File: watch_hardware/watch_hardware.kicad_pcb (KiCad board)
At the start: 4 copper layers, 31.7 x 39.6 mm, 102 parts, among them J1 USB_C_Receptacle_USB2.0_16P, J2 TF_Card, Q1 PMOS, SW1 SW_Push, SW2 SW_Push, SW3 SW_Push, SW4 SW_Push, U1 ESP32-S3, U10 LM2664, U11 TPS65217, U2 TK018F3716, U3 W25Q128JVP, U4 LIS3MDL, U5 LSM6DSOW, U6 AW9523B, U7 LPS22HB, U8 CJC4344H, U9 OPA2192, Y1 Crystal_GND24

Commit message: daily
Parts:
- C11, C15, C16, C22, C26, C4: footprint Capacitor_SMD:C_0603_1608Metric -> Capacitor_SMD:C_0402_1005Metric
- C18, C19, C21, C27, C29, C34, C36, D1, R12, R13, R14, R16, R17, R18, R19, R4, R5, U9: moved to B.Cu
- C28: footprint Capacitor_SMD:C_0603_1608Metric -> Capacitor_SMD:C_0402_1005Metric; moved to B.Cu
- LS1: footprint Connector_PinHeader_1.27mm:PinHeader_1x02_P1.27mm_Vertical -> Connector_PinHeader_1.00mm:PinHeader_1x02_P1.00mm_Vertical
- moved C13 81.5 mm to (192.4, 74.2)
- moved C14 81.5 mm to (192.4, 76.1)
- moved C15 79.4 mm to (192.6, 79.8)
- moved C24 74.9 mm to (187.3, 78.7)
- moved C22 73.3 mm to (187.2, 81.9)
- moved C38 72.3 mm to (170.8, 47.1), turned to 90 degrees
- moved R7 71.2 mm to (166.3, 86.6)
- moved R8 71.2 mm to (166.3, 88.6)
- moved C39 70.1 mm to (167.1, 53.4), turned to 90 degrees
- moved R17 69.5 mm to (170.0, 52.4)
- moved R16 69.3 mm to (170.0, 51.4), turned to 180 degrees
- moved C40 69.2 mm to (165.6, 53.4), turned to 90 degrees
- moved R5 69.1 mm to (165.0, 67.4), turned to -90 degrees
- moved C42 69.1 mm to (167.1, 50.4), turned to -90 degrees
- moved R4 68.6 mm to (164.3, 63.5), turned to 180 degrees
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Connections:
- C19 pad 1: Net-(C19-Pad1) -> GND
- R12 pad 2: Net-(C19-Pad1) -> GND
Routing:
- net +3.3V: track 0.00 -> 57.4 mm, vias 0 -> 2
- net +5V: track 0.00 -> 35.1 mm, vias 0 -> 2
- net +1V0: track 0.00 -> 33.1 mm, vias 0 -> 1
- net +3V3: track 21.5 -> 52.9 mm, vias 7 -> 12
- net /SYS: track 0.00 -> 24.7 mm, vias 0 -> 4
- net +2V0: track 0.00 -> 21.1 mm, vias 0 -> 1
- net -3V3: track 0.00 -> 20.7 mm, vias 0 -> 1
- net Net-(BT1-+): track 0.00 -> 18.8 mm
- net Net-(U11-VDCDC1): track 0.00 -> 18.2 mm
- net Net-(U11-PB_IN): track 0.00 -> 17.1 mm, vias 0 -> 1
- net /-IN_A: track 0.00 -> 14.2 mm
- net Net-(U11-TS): track 0.00 -> 8.89 mm
- net Net-(U11-L1): track 0.00 -> 7.37 mm
- net /+IN_A: track 0.00 -> 7.01 mm
- net Net-(U1-GPIO46): track 1.83 -> 8.54 mm, vias 1 -> 0
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- added copper zone on F.Cu, net Net-(U11-L2)

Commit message: daily
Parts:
- added SCL0: TestPoint, projects:testpoint, B.Cu at (165.9, 49.6)
- added SDA0: TestPoint, projects:testpoint, B.Cu at (165.9, 51.0)
- C1, C2, C3, R1, R2, R3: moved to B.Cu
- SW1, SW2, SW3, SW4: footprint Connector_PinHeader_1.00mm:PinHeader_1x02_P1.00mm_Vertical -> projects:switch_base; moved to B.Cu
- U11: value TPS65217 -> TPS652170
- moved SW4 11.6 mm to (163.2, 47.9)
- moved R2 4.35 mm to (156.5, 81.6), turned to 180 degrees
- moved C3 4.02 mm to (160.3, 80.5), turned to 180 degrees
- moved SW3 3.35 mm to (159.5, 83.1), turned to 180 degrees
- moved R1 2.92 mm to (152.8, 81.7), turned to 180 degrees
- moved C2 2.62 mm to (156.6, 80.5), turned to 180 degrees
- moved SW2 2.15 mm to (155.8, 83.1), turned to 180 degrees
- moved R3 1.86 mm to (160.2, 81.6), turned to 180 degrees
- moved C1 1.52 mm to (152.9, 80.6), turned to 180 degrees
- moved SW1 1.17 mm to (152.1, 83.1), turned to 180 degrees
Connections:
- C39 pad 2: Net-(U11-VDCDC1) -> +3.3V
- C40 pad 2: Net-(U11-VDCDC1) -> +3.3V
- C43 pad 2: +1V0 -> +3.3VDAC
- C44 pad 2: +1V0 -> +3.3VDAC
- L2 pad 1: Net-(U11-VDCDC1) -> +3.3V
- L4 pad 2: +1V0 -> +3.3VDAC
- U11 pad 19: Net-(U11-VDCDC1) -> +3.3V
- U11 pad 29: +1V0 -> +3.3VDAC
- U11 pad 39: +3V3 -> unconnected-(U11-LS1_IN-Pad39)
- U11 pad 40: +3.3VDAC -> unconnected-(U11-LS1_OUT-Pad40)
- U11 pad 42: +3V3 -> unconnected-(U11-LS2_IN-Pad42)
- U11 pad 43: +3.3V -> unconnected-(U11-LS2_OUT-Pad43)
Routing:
- net /L_CS: track 2.13 -> 20.6 mm
- net Net-(U11-PB_IN): track 17.1 -> 6.65 mm
- net /L_RST: track 2.04 -> 11.3 mm
- net /SDA0: track 6.59 -> 12.6 mm
- net /SCL0: track 6.55 -> 12.1 mm
- net +3V3: track 52.9 -> 48.6 mm
- net unconnected-(U11-LS2_IN-Pad42): track 0.00 -> 3.29 mm
- net unconnected-(U11-LS1_OUT-Pad40): track 0.00 -> 2.90 mm
- net +3.3VDAC: track 6.05 -> 3.15 mm
- net /L_D1: track 13.8 -> 16.2 mm
- net unconnected-(U11-LS1_IN-Pad39): track 0.00 -> 1.00 mm
- net GND: vias 74 -> 73

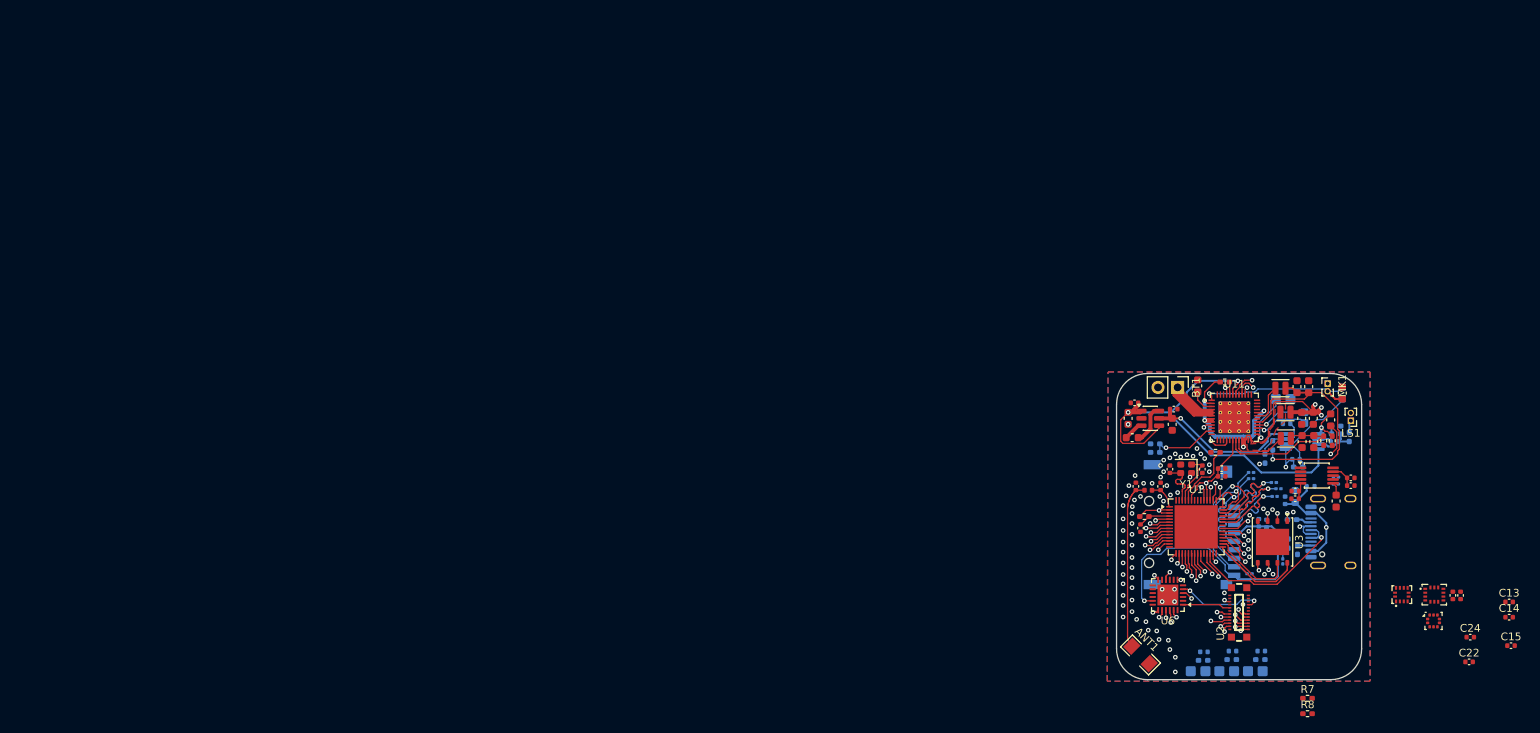
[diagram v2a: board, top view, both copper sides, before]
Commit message: 准备添加卫星定位
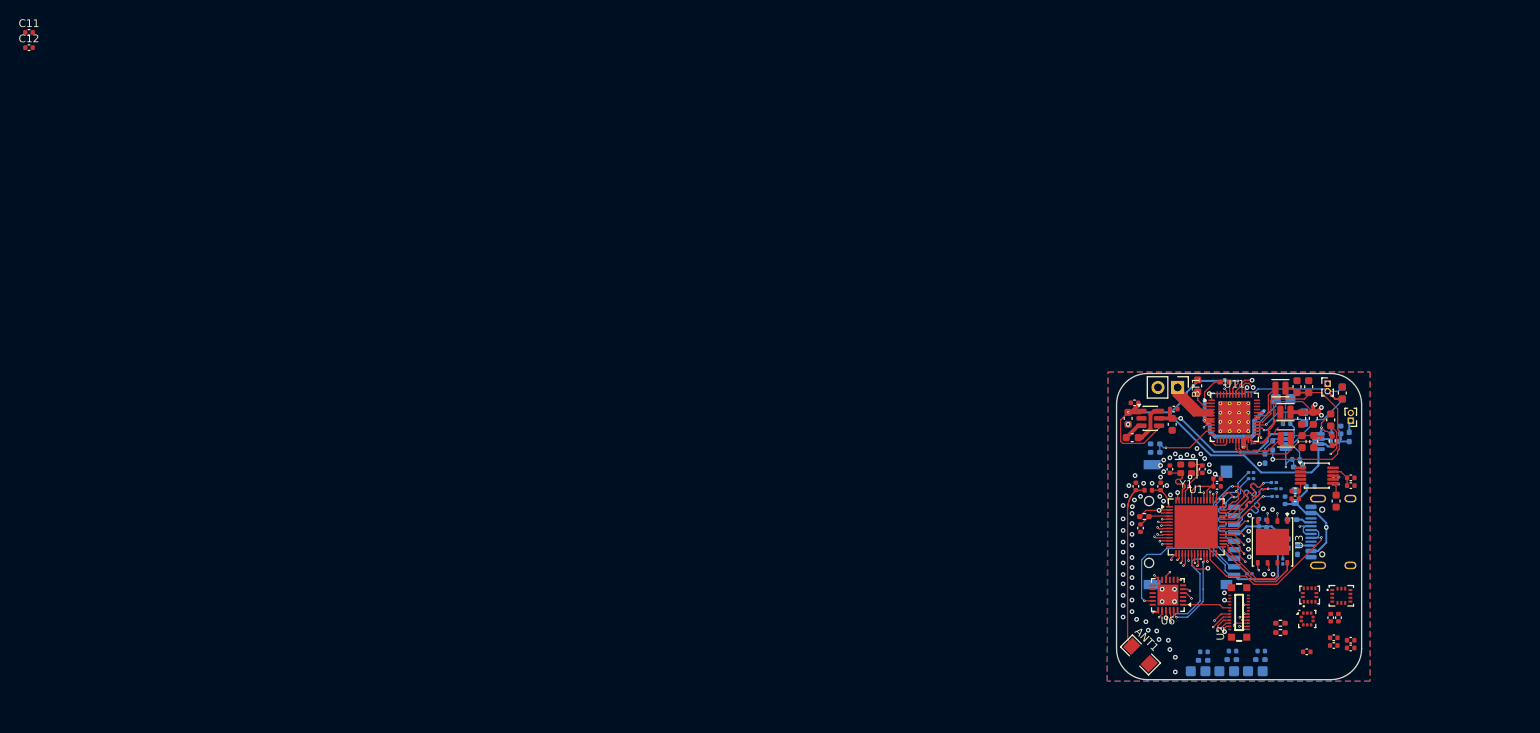
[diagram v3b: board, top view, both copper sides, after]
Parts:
- removed the R11 at (154.4, 54.8)
- removed R22: 10k, Resistor_SMD:R_0402_1005Metric_Pad0.72x0.64mm_HandSolder
- added C11: 100nF, Capacitor_SMD:C_0402_1005Metric, F.Cu at (0.94, 0.48)
- added C12: 10uF, Capacitor_SMD:C_0402_1005Metric, F.Cu at (0.94, 2.46)
- R10: renamed from R13; value 82k -> 270k
- moved C15 27.0 mm to (166.2, 80.6)
- moved C17 20.7 mm to (171.9, 80.1)
- moved C16 20.7 mm to (171.9, 79.1)
- moved C26 17.7 mm to (169.7, 78.8)
- moved C24 17.6 mm to (169.7, 79.8)
- moved U7 16.3 mm to (166.3, 76.3)
- moved C13 16.1 mm to (170.3, 76.2)
- moved C14 16.1 mm to (169.3, 76.2)
- moved U5 12.0 mm to (170.7, 73.3)
- moved U4 11.9 mm to (166.6, 73.2)
- moved R8 11.1 mm to (162.8, 78.1)
- moved R7 10.3 mm to (162.8, 76.9)
- moved C4 1.43 mm to (154.6, 58.2)
- moved C6 1.43 mm to (154.6, 59.2)
- renumbered C11 to C13, C12 to C14, C13 to C15, C14 to C16, C15 to C17, C16 to C18, C17 to C19, C18 to C20, C19 to C21, C20 to C22, C21 to C23, C22 to C24, C23 to C25, C24 to C26, C25 to C27, C26 to C28, C27 to C29, C28 to C30, C29 to C31, C30 to C32, C31 to C33, C32 to C34, C33 to C35, C34 to C36, C35 to C37, C36 to C38, C37 to C39, C38 to C40, C39 to C41, C40 to C42, C41 to C43, C42 to C44, C43 to C45, C44 to C46, R14 to R11, R15 to R12, R16 to R13, R17 to R14, R18 to R15, R19 to R16, R20 to R17, R21 to R18, R12 to R9, SCL0 to SCL1, SDA0 to SDA1
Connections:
- C16 pad 1: +3.3VA -> +3.3VP
- C17 pad 1: +3.3VA -> +3.3VP
- C24 pad 1: +3.3VA -> +3.3VP
- C26 pad 1: +3.3VA -> +3.3VP
- R10 pad 1: +1V0 -> +2V0
- U1 pad 20: +3V3 -> +3.3VA
- U1 pad 24: unconnected-(U1-GPIO18-Pad24) -> /AW_RST
- U1 pad 27: /AW_RST -> unconnected-(U1-GPIO21-Pad27)
- U1 pad 52: Net-(U1-GPIO46) -> GND
- U11 pad 39: unconnected-(U11-LS1_IN-Pad39) -> +3V3
- U11 pad 40: unconnected-(U11-LS1_OUT-Pad40) -> +3.3VP
- U4 pad 10: +3.3VA -> +3.3VP
- U4 pad 5: +3.3VA -> +3.3VP
- U4 pad 6: +3.3VA -> +3.3VP
- U5 pad 5: +3.3VA -> +3.3VP
- U7 pad 1: +3.3VA -> +3.3VP
- U7 pad 10: +3.3VA -> +3.3VP
- U7 pad 6: +3.3VA -> +3.3VP
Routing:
- net +1V0: track 33.1 -> 0.00 mm, vias 1 -> 0
- net (no net): track 0.00 -> 33.1 mm
- net +3.3V: track 57.4 -> 75.6 mm
- net Net-(U11-VDCDC1): track 18.2 -> 0.00 mm
- net /L_RST: track 11.3 -> 1.53 mm
- net /AW_INT: track 4.90 -> 14.5 mm
- net /AW_RST: track 2.28 -> 11.6 mm
- net Net-(U1-GPIO46): track 8.54 -> 0.00 mm
- net +3V3: track 48.6 -> 42.3 mm, vias 12 -> 11
- net /L_CS: track 20.6 -> 16.4 mm
- net +3.3VA: track 3.20 -> 7.03 mm, vias 0 -> 1
- net /L_MOSI: track 19.3 -> 15.5 mm
- net unconnected-(U11-LS1_OUT-Pad40): track 2.90 -> 0.00 mm
- net +3.3VP: track 0.00 -> 2.90 mm
- net /GPIO2: track 3.20 -> 1.08 mm
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
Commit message: 完成电路设计
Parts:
- removed C11: 100nF, Capacitor_SMD:C_0402_1005Metric
- removed C12: 10uF, Capacitor_SMD:C_0402_1005Metric
- added AE1: IPEX_1, projects:IPEX_1, F.Cu at (167.7, 82.1)
- added C32: 100nF, Capacitor_SMD:C_0402_1005Metric, B.Cu at (165.0, 81.2)
- added C33: 470pF, Capacitor_SMD:C_0402_1005Metric, B.Cu at (166.7, 81.9)
- added C34: 100nF, Capacitor_SMD:C_0402_1005Metric, B.Cu at (167.7, 78.2)
- added C35: 470pF, Capacitor_SMD:C_0402_1005Metric, B.Cu at (159.6, 76.1)
- added C37: 10nF, Capacitor_SMD:C_0402_1005Metric, B.Cu at (167.3, 74.5)
- added C38: 10nF, Capacitor_SMD:C_0402_1005Metric, B.Cu at (168.9, 72.4)
- added C40: 100nF, Capacitor_SMD:C_0402_1005Metric, B.Cu at (166.6, 73.0)
- added C41: 100nF, Capacitor_SMD:C_0402_1005Metric, B.Cu at (166.6, 71.5)
- added C42: 470pF, Capacitor_SMD:C_0402_1005Metric, B.Cu at (163.9, 71.1)
- added C43: 100nF, Capacitor_SMD:C_0402_1005Metric, B.Cu at (162.1, 71.3)
- added C44: 100nF, Capacitor_SMD:C_0402_1005Metric, B.Cu at (159.0, 77.6)
- added C45: 10nF, Capacitor_SMD:C_0402_1005Metric, B.Cu at (160.0, 77.6)
- added L2: 47nH, Inductor_SMD:L_0402_1005Metric, B.Cu at (167.7, 81.9)
- added R17: 20k, Resistor_SMD:R_0402_1005Metric_Pad0.72x0.64mm_HandSolder, B.Cu at (163.8, 72.1)
- added U10: MAX2769C, Package_DFN_QFN:QFN-28-1EP_5x5mm_P0.5mm_EP3.25x3.25mm_ThermalVias, B.Cu at (163.7, 77.1)
- added Y2: 7Q16300001, Crystal:Crystal_SMD_3225-4Pin_3.2x2.5mm, B.Cu at (170.2, 75.5)
- C39: value 10uF -> 27pF; footprint Capacitor_SMD:C_0603_1608Metric -> Capacitor_SMD:C_0402_1005Metric; moved to B.Cu
- moved C39 29.4 mm to (163.9, 73.1), turned to 180 degrees
- moved C54 18.7 mm to (152.1, 46.2)
- moved C24 9.58 mm to (160.7, 76.5), turned to -90 degrees
- moved D2 8.60 mm to (164.1, 64.3)
- moved D3 8.47 mm to (164.2, 65.0)
- moved C26 8.32 mm to (161.7, 76.5), turned to -90 degrees
- moved C15 5.89 mm to (167.2, 74.8), turned to -90 degrees
- moved C17 5.80 mm to (169.3, 74.9), turned to -90 degrees
- moved U7 5.73 mm to (161.0, 74.1), turned to 180 degrees
- moved C16 5.52 mm to (168.3, 74.9), turned to -90 degrees
- moved R7 4.55 mm to (163.5, 72.4), turned to 180 degrees
- moved R8 4.55 mm to (163.5, 73.6), turned to 180 degrees
- moved C14 3.22 mm to (172.3, 75.0), turned to -90 degrees
- moved C3 2.91 mm to (161.8, 83.0), turned to -90 degrees
- moved C6 1.71 mm to (155.2, 57.6), turned to 90 degrees
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- renumbered C32 to C46, C33 to C47, C34 to C48, C35 to C49, C36 to C50, C37 to C51, C38 to C52, C40 to C54, C41 to C55, C42 to C56, C43 to C57, C44 to C58, C45 to C59, C46 to C60, L2 to L3, L3 to L4, L4 to L5, R17 to R18, R18 to R19, U10 to U11, U11 to U12
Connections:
- C13 pad 1: +3.3VA -> +3.3VP
- C14 pad 1: +3.3VA -> +3.3VP
- C39 pad 1: GND -> Net-(U10-CPOUT)
- C39 pad 2: +3.3VA -> GND
- C54 pad 1: +2V0 -> +3.3VADC
- U1 pad 14: unconnected-(U1-GPIO9-Pad14) -> /MAX_I1
- U1 pad 20: +3.3VA -> +3V3
- U1 pad 27: unconnected-(U1-GPIO21-Pad27) -> /MAX_I0
- U1 pad 36: unconnected-(U1-SPICLK_N/GPIO48-Pad36) -> /MAX_Q0
- U1 pad 43: /I2s_SD -> /I2s_MCLK
- U1 pad 44: /I2s_BCK -> /I2s_WS
- U1 pad 45: /I2s_WS -> /I2s_BCK
- U1 pad 47: /I2s_MCLK -> /I2s_SD
- U1 pad 48: unconnected-(U1-MTMS/JTAG/GPIO42-Pad48) -> /MAX_Q1
- U1 pad 49: unconnected-(U1-U0TXD-Pad49) -> /ADC_CLK
- U1 pad 50: unconnected-(U1-U0RXD-Pad50) -> /MAX_CS
- U12 pad 1: +2V0 -> +3.3VADC
- U12 pad 3: +3.3VA -> unconnected-(U12-VLDO1-Pad3)
- U12 pad 42: unconnected-(U11-LS2_IN-Pad42) -> +3V3
- U12 pad 43: unconnected-(U11-LS2_OUT-Pad43) -> +2V0
- U5 pad 12: +3.3VA -> +3.3VP
- U5 pad 8: +3.3VA -> +3.3VP
- U6 pad 16: unconnected-(U6-P1_6-Pad16) -> /MAX_IDLE
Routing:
- net +3V3: track 42.3 -> 231.3 mm, vias 11 -> 18
- net /SCL0: track 11.6 -> 123.7 mm, vias 4 -> 7
- net +3.3VADC: track 0.00 -> 106.8 mm, vias 0 -> 7
- net /SDA0: track 11.9 -> 97.5 mm, vias 4 -> 8
- net +3.3VP: track 2.90 -> 74.6 mm, vias 0 -> 2
- net /LSM_INT: track 0.79 -> 51.2 mm, vias 1 -> 2
- net GND: track 0.00 -> 44.3 mm, vias 73 -> 149
- net /MAX_Q1: track 0.00 -> 37.2 mm, vias 0 -> 2
- net /MAX_IDLE: track 0.00 -> 34.9 mm, vias 0 -> 2
- net /GPIO3: track 1.66 -> 35.7 mm
- net /ADC_CLK: track 0.00 -> 33.9 mm, vias 0 -> 2
- net /MAX_I1: track 0.00 -> 33.5 mm, vias 0 -> 2
- net (no net): track 33.1 -> 0.00 mm
- net /GPIO1: track 1.50 -> 33.0 mm, vias 1 -> 2
- net /GPIO2: track 1.08 -> 32.1 mm
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- removed copper zone on F.Cu, net Net-(U12-L2)

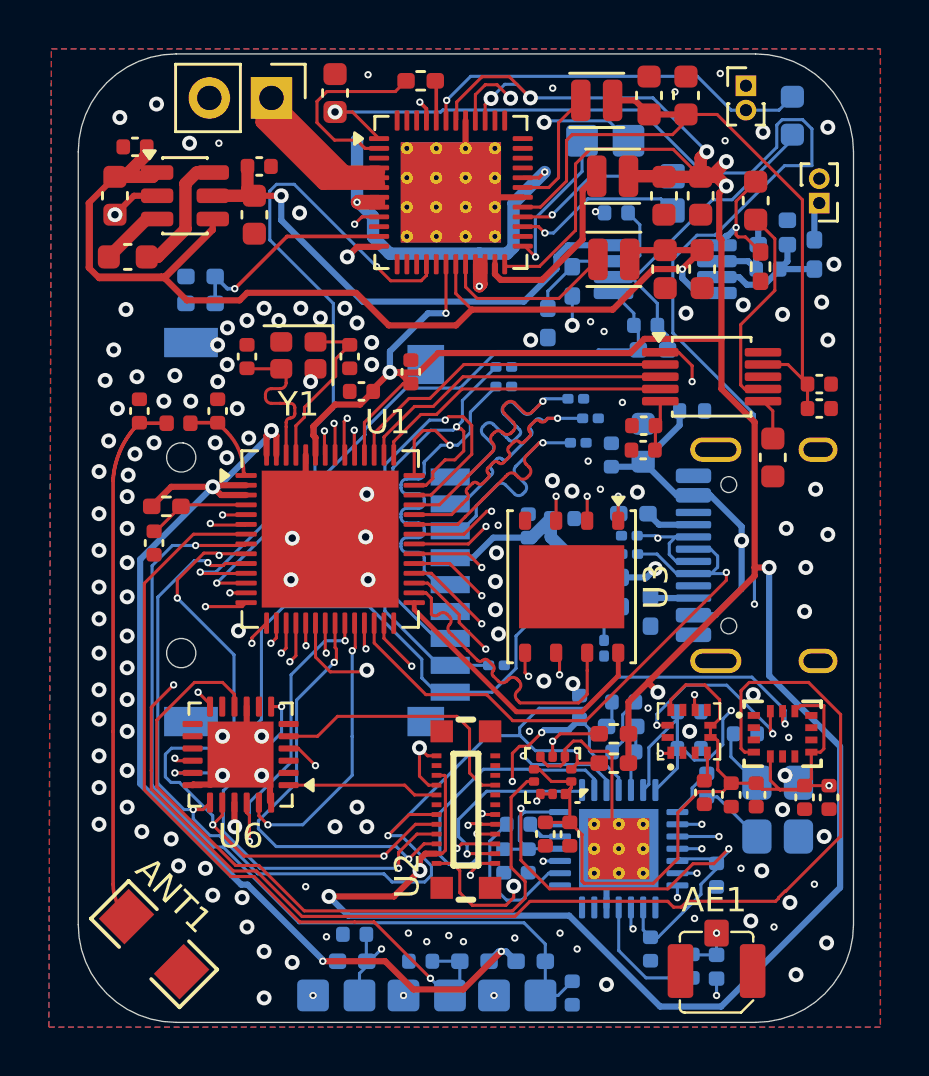
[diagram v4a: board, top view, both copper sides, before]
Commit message: 修改电路设计，未完成，还需修改，以符合生产需求
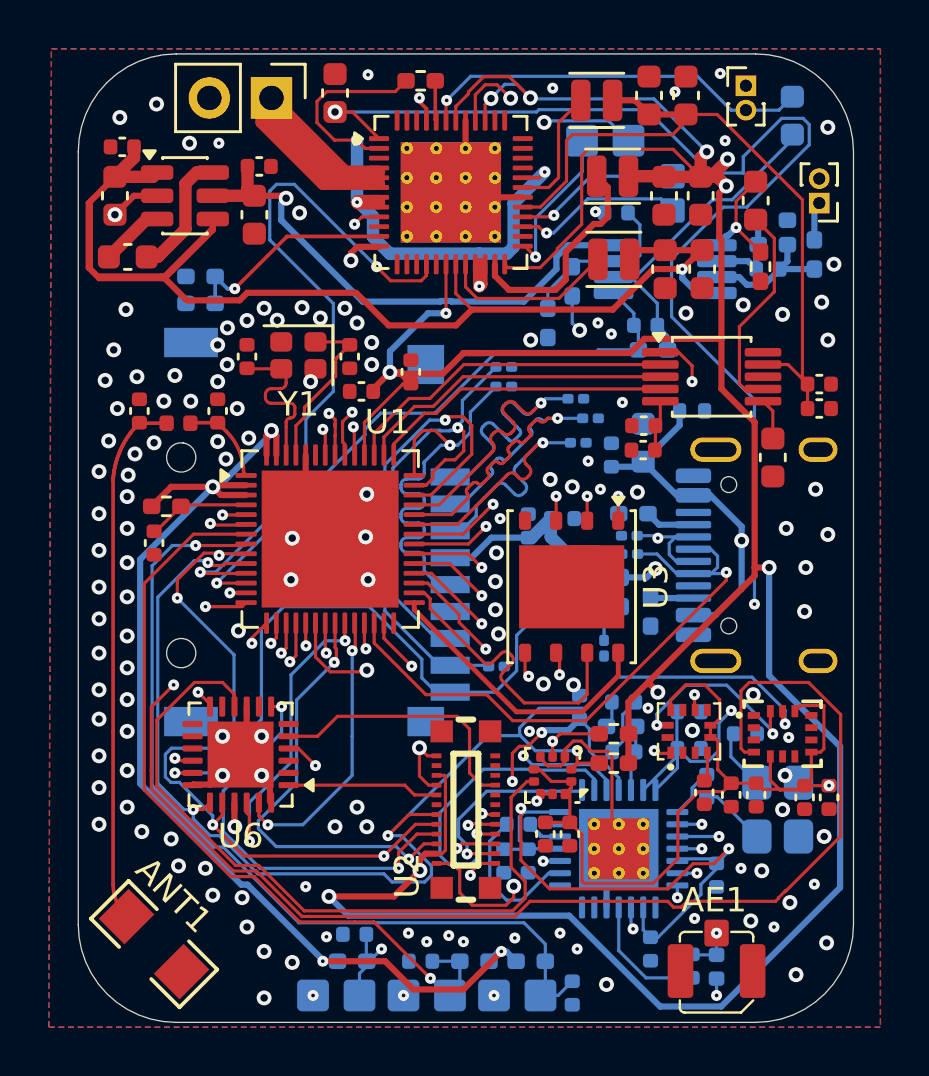
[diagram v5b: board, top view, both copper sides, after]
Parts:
- moved C47 0.52 mm to (143.4, 48.4)
- moved D9 0.05 mm to (158.7, 69.7)
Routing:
- net /SCL0: track 123.7 -> 111.6 mm
- net +3.3VADC: track 106.8 -> 103.4 mm
- net +3V3: track 231.3 -> 228.4 mm
- net Net-(U12-L2): track 7.60 -> 9.08 mm
- net +5V: track 40.2 -> 41.0 mm
- net +2V0: track 29.5 -> 30.2 mm
- net /PMIC_INT: track 22.4 -> 23.0 mm
- net /MAX_Q1: track 37.2 -> 37.7 mm
- net /ADC_CLK: track 33.9 -> 34.4 mm
- net GND: vias 149 -> 148
